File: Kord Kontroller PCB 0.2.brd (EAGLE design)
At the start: 242.5 x 100 mm, 187 parts, among them IC2 74HCT1G125DBV, J1 MIDIOUTB, J2 MIDIOUTA, J3 FTSH-105-01-L-DV-KJ, SW2 SPST_TACT-KMR2, U1 AP2112K-3.3, U2 ATSAMD51J19A-AUT, X3 microUSB

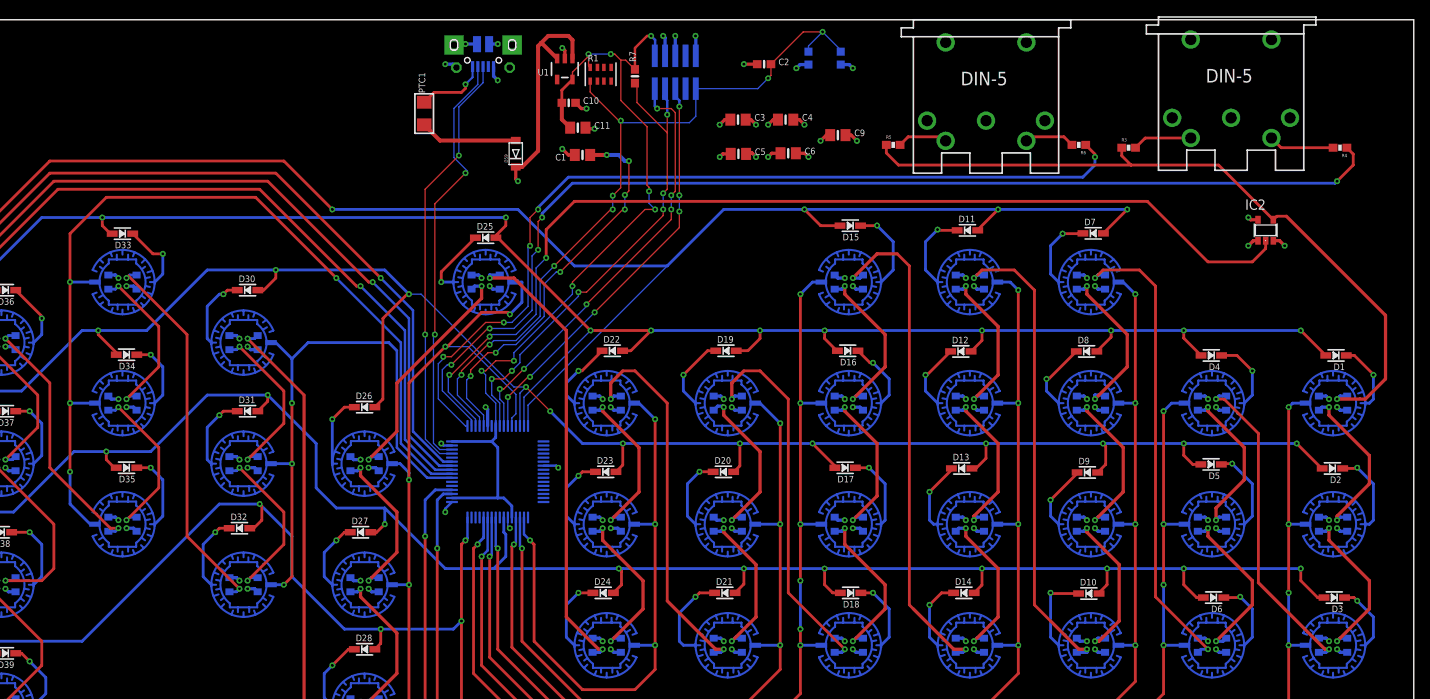
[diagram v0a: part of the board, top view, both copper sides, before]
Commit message: Switched pieces to bottom
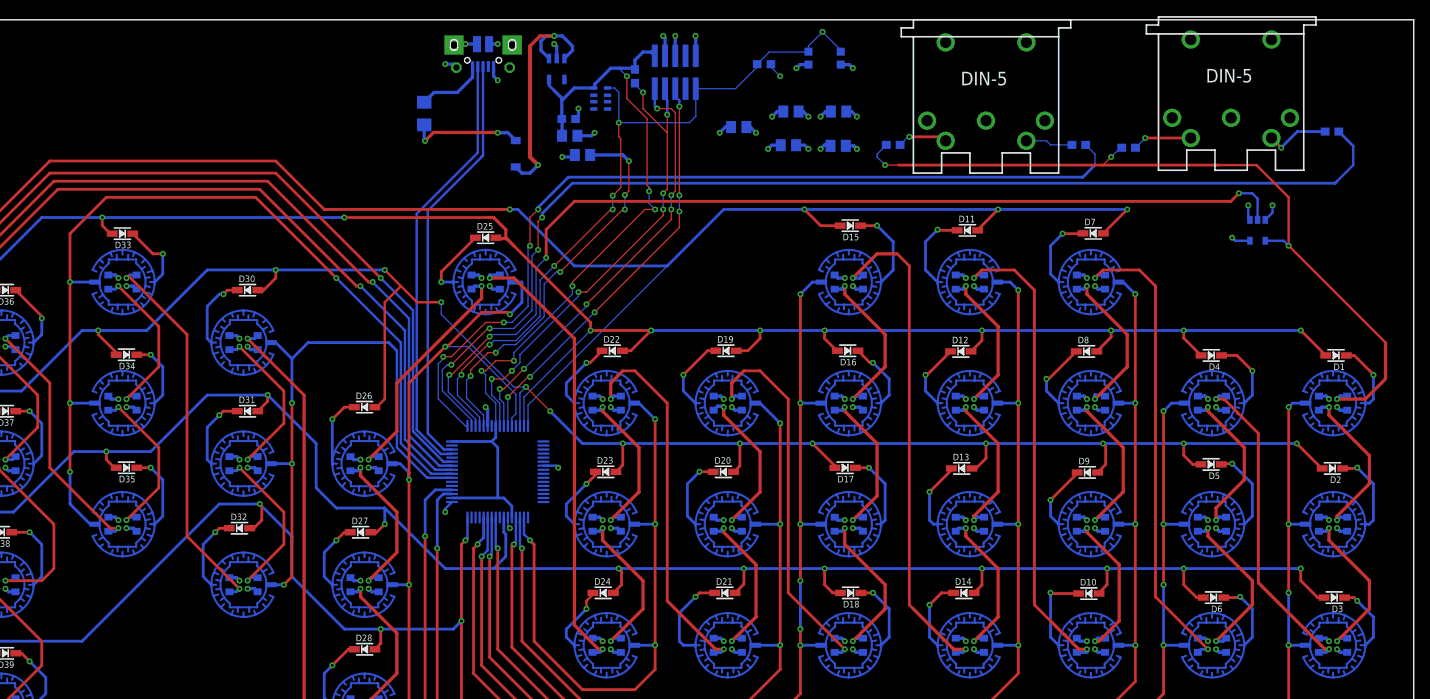
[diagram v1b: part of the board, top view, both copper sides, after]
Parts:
- moved C3 12.5 mm to (171.2, 88.6), flipped to the bottom
- moved C5 12.4 mm to (171.2, 84.4), flipped to the bottom
- moved C9 12.3 mm to (158.9, 86.7), flipped to the bottom
- moved R1 3.00 mm to (141.8, 90.2), flipped to the bottom, turned to 270 degrees
- moved R4 2.24 mm to (232.4, 86.2), flipped to the bottom, turned to 0 degrees
- moved C10 2.00 mm to (137.8, 87.7), flipped to the bottom, turned to 180 degrees
- moved C11 1.41 mm to (137.9, 85.6), flipped to the bottom, turned to 180 degrees
- moved C4 1.20 mm to (165.3, 88.6), flipped to the bottom
- moved C6 1.00 mm to (165.0, 84.5), flipped to the bottom
- moved IC2 1.00 mm to (223.2, 73.9), flipped to the bottom, turned to 180 degrees
- moved U1 1.00 mm to (136.3, 93.9), flipped to the bottom
- flipped C1 to the bottom, turned to 0 degrees
- flipped C2 to the bottom
- flipped D59 to the bottom
- flipped PTC1 to the bottom
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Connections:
- net D+: now also U2.46; no longer U2.45
- net D-: now also U2.45; no longer U2.46
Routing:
- net LEVELSHIFT_5V: track 90.8 -> 97.9 mm, vias 1 -> 4
- net 3.3V: track 109.9 -> 104.8 mm, vias 8 -> 6
- net NRESET: track 95.4 -> 91.0 mm, vias 8 -> 7
- net VDD: track 113.6 -> 117.5 mm, vias 61 -> 62
- net LEVELSHIFT_3V: track 128.2 -> 125.7 mm, vias 3 -> 4
- net MIDIOUTA: track 140.7 -> 143.1 mm, vias 5 -> 4
- net VBUS: track 12.1 -> 14.1 mm, vias 0 -> 2
- net ROW2: track 315.6 -> 316.8 mm, vias 17 -> 18
- net D+: track 53.2 -> 52.1 mm, vias 2 -> 0
- net N$62: track 9.34 -> 8.27 mm
- net N$58: track 9.35 -> 8.40 mm
- net D-: track 53.1 -> 53.8 mm, vias 2 -> 0
- net N$66: track 8.21 -> 8.60 mm, vias 1 -> 0
- net GND: track 133.6 -> 134.0 mm, vias 80 -> 79
- net SWDCLK: track 61.1 -> 61.5 mm, vias 6 -> 7
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
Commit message: Added osc and reourting diodes
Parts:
- added C7, C8: 10uF, microbuilder:0805-NO
- added Q1: ASFL, crystal:ASF
- moved D3 44.7 mm to (240.7, 72.4), flipped to the bottom, turned to 270 degrees
- moved D2 30.6 mm to (238.6, 74.4), flipped to the bottom, turned to 270 degrees
- moved D5 18.1 mm to (215.4, 62.9), flipped to the bottom, turned to 0 degrees
- moved D6 15.1 mm to (219.7, 13.4), flipped to the bottom, turned to 270 degrees
- moved D1 14.3 mm to (235.9, 72.4), flipped to the bottom, turned to 90 degrees
- moved D4 8.25 mm to (215.4, 66.4), flipped to the bottom, turned to 0 degrees
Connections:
- new net N$63: C8.1, Q1.4
- new net N$69: C7.1, Q1.2
- new net OSCIN: Q1.1, U2.1
- new net OSCOUT: Q1.3, U2.2
- net GND: now also C7.2, C8.2
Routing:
- net ROW3: track 301.9 -> 367.5 mm, vias 15 -> 19
- net N$25: track 8.49 -> 61.6 mm, vias 1 -> 4
- net ROW2: track 316.8 -> 359.0 mm, vias 18 -> 20
- net N$20: track 10.4 -> 42.4 mm, vias 1 -> 2
- net N$22: track 10.3 -> 31.4 mm, vias 1 -> 4
- net N$6: track 8.59 -> 20.0 mm, vias 1 -> 0
- net N$9: track 9.02 -> 16.7 mm, vias 1 -> 0
- net ROW1: track 295.9 -> 302.1 mm
- net LEVELSHIFT_5V: track 97.9 -> 92.6 mm
- net COL2: track 159.9 -> 161.6 mm
- net N$13: track 40.5 -> 41.1 mm
- net N$26: track 9.11 -> 8.98 mm, vias 1 -> 0

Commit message: Moved resistors to bottom and Added 32k crystal
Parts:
- Q1: value ASFL -> (none); device crystal:ASF -> special:QS
- moved C8 132.2 mm to (132.0, 19.0), flipped to the bottom, turned to 180 degrees
- moved C7 132.1 mm to (133.0, 15.0), flipped to the bottom, turned to 180 degrees
- moved Q1 123.7 mm to (132.0, 26.0), flipped to the bottom, turned to 270 degrees
- moved D48 42.4 mm to (33.5, 2.50), flipped to the bottom
- moved D17 37.1 mm to (170.0, 7.49), flipped to the bottom, turned to 0 degrees
- moved D52 36.9 mm to (16.0, 79.5), flipped to the bottom, turned to 180 degrees
- moved D9 36.7 mm to (195.1, 7.91), flipped to the bottom
- moved D13 36.3 mm to (181.5, 8.41), flipped to the bottom, turned to 180 degrees
- moved D20 35.4 mm to (152.0, 8.99), flipped to the bottom
- moved D37 33.5 mm to (74.0, 84.5), flipped to the bottom
- moved D23 32.6 mm to (157.4, 73.0), flipped to the bottom, turned to 180 degrees
- moved D49 30.5 mm to (39.0, 2.50), flipped to the bottom, turned to 180 degrees
- moved D38 29.8 mm to (86.5, 13.5), flipped to the bottom
- moved D44 28.6 mm to (43.5, 71.5), flipped to the bottom, turned to 180 degrees
- moved D41 28.3 mm to (57.0, 71.5), flipped to the bottom
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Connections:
- removed net N$63: C8.1, Q1.4
- removed net N$69: C7.1, Q1.2
- net OSCIN: now also C8.1
- net OSCOUT: now also C7.1, Q1.2; no longer Q1.3
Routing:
- net ROW2: track 359.0 -> 669.5 mm, vias 20 -> 30
- net ROW3: track 367.5 -> 634.2 mm, vias 19 -> 26
- net ROW1: track 302.1 -> 440.5 mm, vias 15 -> 10
- net ROW4: track 172.3 -> 256.0 mm, vias 6 -> 9
- net OSCOUT: track 0.00 -> 41.2 mm, vias 0 -> 2
- net OSCIN: track 0.00 -> 41.0 mm, vias 0 -> 5
- net N$58: track 8.40 -> 48.4 mm, vias 1 -> 4
- net N$126: track 8.89 -> 48.1 mm, vias 1 -> 2
- net N$84: track 9.27 -> 46.0 mm, vias 1 -> 4
- net N$125: track 9.68 -> 46.1 mm, vias 1 -> 4
- net N$123: track 9.18 -> 39.8 mm, vias 1 -> 4
- net N$124: track 8.39 -> 38.4 mm, vias 1 -> 2
- net N$52: track 8.73 -> 38.1 mm, vias 1 -> 2
- net N$83: track 8.77 -> 37.6 mm, vias 1 -> 4
- net N$18: track 8.44 -> 35.9 mm, vias 1 -> 2
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
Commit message: Moved resistor a little
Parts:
- moved D29 1.41 mm to (143.5, 3.00)
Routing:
- net N$70: track 12.0 -> 12.6 mm
- net ROW4: track 256.0 -> 256.5 mm
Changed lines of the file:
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@@
 <attribute name="VALUE" x="145.238" y="94.778" size="0.4064" layer="28" font="vector" ratio="10" rot="MR90"/>
 </element>
-<element name="D29" library="microbuilder" package="SOD-323" value="1N4148" x="142.5" y="2" smashed="yes" rot="MR180">
-<attribute name="NAME" x="141.4" y="1" size="0.8128" layer="26" ratio="18" rot="MR180"/>
-<attribute name="VALUE" x="141.4" y="3.792" size="0.4064" layer="28" ratio="10" rot="MR180"/>
+<element name="D29" library="microbuilder" package="SOD-323" value="1N4148" x="143.5" y="3" smashed="yes" rot="MR180">
+<attribute name="NAME" x="142.4" y="2" size="0.8128" layer="26" ratio="18" rot="MR180"/>
+<attribute name="VALUE" x="142.4" y="4.792" size="0.4064" layer="28" ratio="10" rot="MR180"/>
 </element>
 <element name="B29" library="microbuilder" package="ELAST_PAD_SQUARE_10MM_4X4WIDE" value="ELAST_10X10" x="127.5" y="7.5" smashed="yes" rot="MR180"/>
@@
 <wire x1="125.25" y1="38.33" x2="125.25" y2="37.75" width="0.3048" layer="16"/>
 <wire x1="125.25" y1="37.75" x2="124" y2="36.5" width="0.3048" layer="16"/>
-<wire x1="143.77" y1="2" x2="141.77" y2="4" width="0.3048" layer="16"/>
-<wire x1="141.77" y1="4" x2="141" y2="4" width="0.3048" layer="16"/>
+<wire x1="144.77" y1="3" x2="142.77" y2="5" width="0.3048" layer="16"/>
+<wire x1="142.77" y1="5" x2="140" y2="5" width="0.3048" layer="16"/>
 <wire x1="126" y1="19" x2="122.5" y2="19" width="0.3048" layer="16"/>
 <via x="122.5" y="19" extent="1-16" drill="0.35"/>
-<wire x1="141" y1="4" x2="126" y2="19" width="0.3048" layer="16"/>
+<wire x1="140" y1="5" x2="126" y2="19" width="0.3048" layer="16"/>
 <wire x1="96.77" y1="3" x2="98.77" y2="5" width="0.3048" layer="16"/>
 <wire x1="98.77" y1="5" x2="99" y2="5" width="0.3048" layer="16"/>
@@
 <contactref element="D29" pad="C"/>
 <contactref element="B29" pad="P$2"/>
-<wire x1="131.5" y1="7.5" x2="137" y2="2" width="0.3048" layer="16"/>
-<wire x1="137" y1="2" x2="141.23" y2="2" width="0.3048" layer="16"/>
+<wire x1="131.5" y1="7.5" x2="136" y2="3" width="0.3048" layer="16"/>
+<wire x1="136" y1="3" x2="142.23" y2="3" width="0.3048" layer="16"/>
 </signal>
 <signal name="OSCIN">

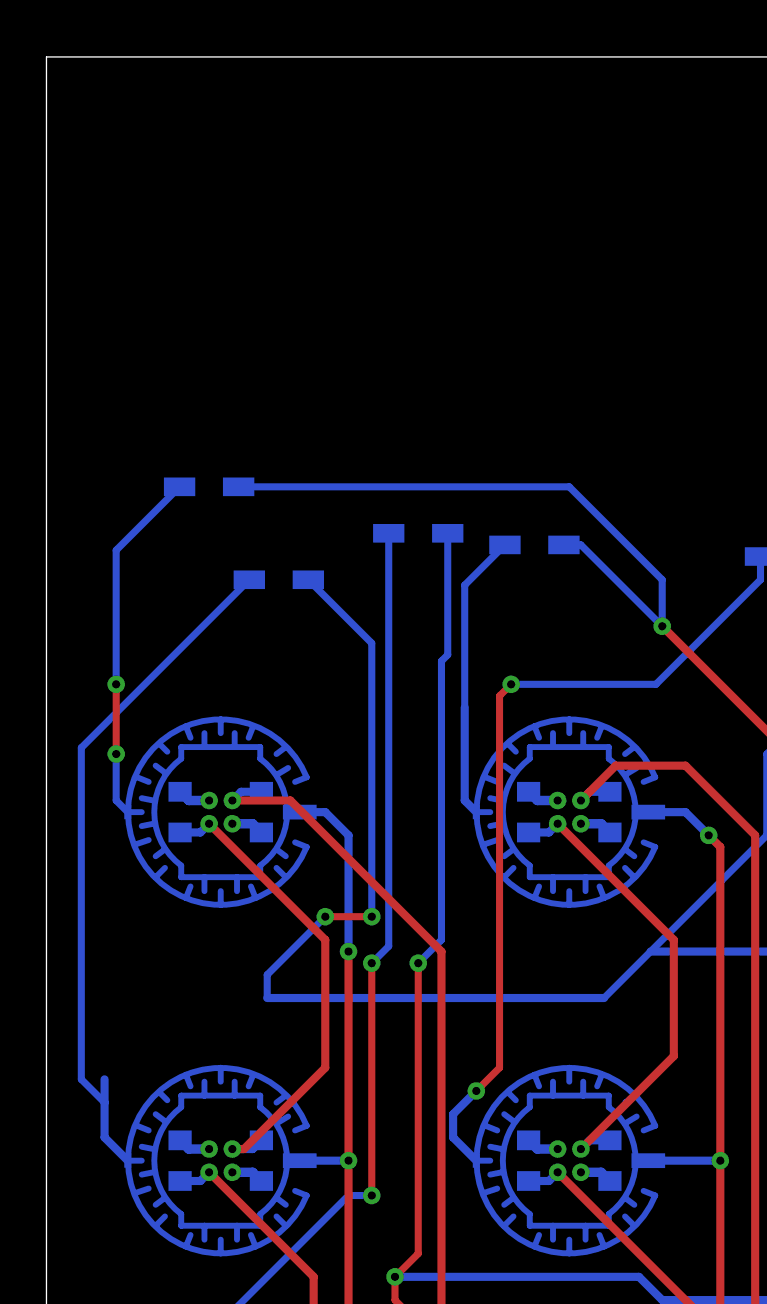
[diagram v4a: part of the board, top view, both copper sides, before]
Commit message: added a logo
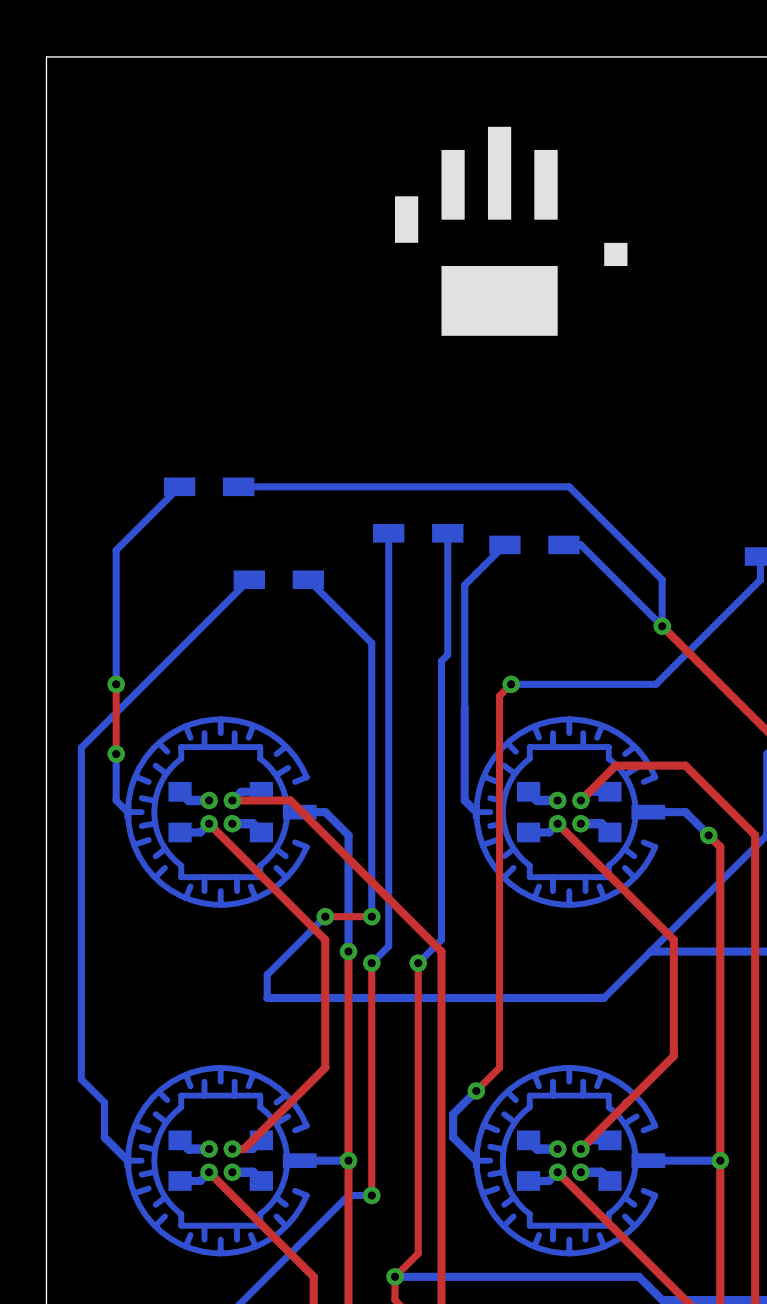
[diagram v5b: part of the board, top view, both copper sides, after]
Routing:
- net N$122: track 29.8 -> 28.8 mm
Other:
- board text added: "Kord Kontroller"
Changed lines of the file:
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@@
 <setting verticaltext="up"/>
 </settings>
-<grid distance="1" unitdist="mm" unit="mm" style="lines" multiple="1" display="yes" altdistance="1" altunitdist="mm" altunit="mm"/>
+<grid distance="7.5" unitdist="mm" unit="mm" style="lines" multiple="1" display="yes" altdistance="1" altunitdist="mm" altunit="mm"/>
 <layers>
 <layer number="1" name="Top" color="4" fill="1" visible="yes" active="yes"/>
@@
 <wire x1="242.5" y1="100" x2="0" y2="100" width="0" layer="20"/>
 <wire x1="0" y1="100" x2="0" y2="0" width="0" layer="20"/>
+<text x="27.75" y="96" size="7" layer="22" font="fixed" rot="MR180">Kord Kontroller</text>
+<rectangle x1="17" y1="88" x2="22" y2="91" layer="21"/>
+<rectangle x1="24" y1="91" x2="25" y2="92" layer="21"/>
+<rectangle x1="21" y1="93" x2="22" y2="96" layer="21"/>
+<rectangle x1="19" y1="93" x2="20" y2="97" layer="21"/>
+<rectangle x1="17" y1="93" x2="18" y2="96" layer="21"/>
+<rectangle x1="15" y1="92" x2="16" y2="94" layer="21"/>
 </plain>
 <attributes>
@@
 <contactref element="D51" pad="C"/>
 <contactref element="B51" pad="P$2"/>
-<wire x1="2.5" y1="56" x2="2.5" y2="55" width="0.35" layer="16"/>
-<wire x1="2.5" y1="55" x2="2.5" y2="53.5" width="0.35" layer="16"/>
-<wire x1="3.5" y1="52.5" x2="2.5" y2="53.5" width="0.35" layer="16"/>
+<wire x1="2.5" y1="53.5" x2="3.5" y2="52.5" width="0.35" layer="16"/>
 <wire x1="8.73" y1="77.5" x2="1.5" y2="70.27" width="0.3048" layer="16"/>
 <wire x1="1.5" y1="70.27" x2="1.5" y2="56" width="0.3048" layer="16"/>
 <wire x1="1.5" y1="56" x2="2.5" y2="55" width="0.3048" layer="16"/>
+<wire x1="2.5" y1="55" x2="2.5" y2="53.5" width="0.3048" layer="16"/>
 </signal>
 <signal name="N$123">
